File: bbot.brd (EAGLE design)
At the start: 61.5 x 53.3 mm, 27 parts

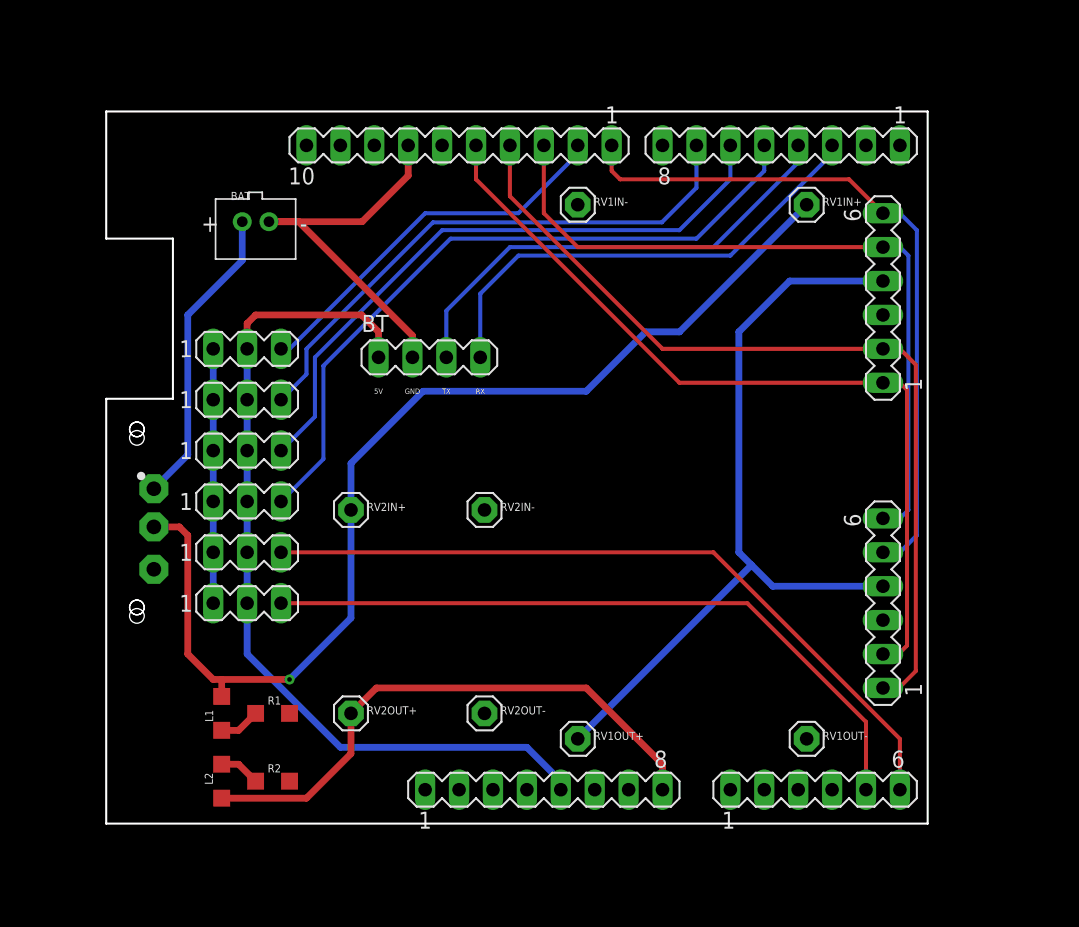
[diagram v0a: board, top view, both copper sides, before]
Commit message: added lm2596, everything is working
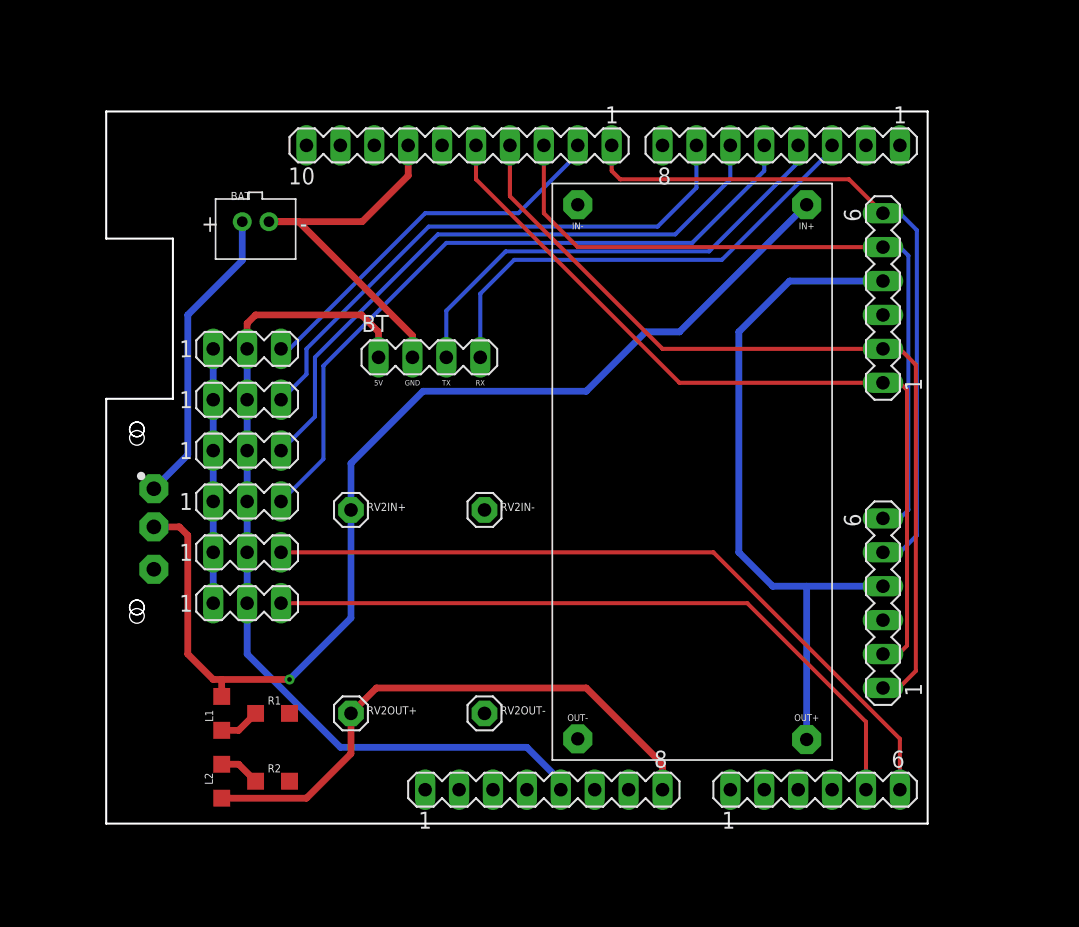
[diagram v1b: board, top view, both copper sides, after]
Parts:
- removed RV1IN+, RV1IN-, RV1OUT+, RV1OUT-: (no value), adafruit:1X01
- added U$1: BB-LM2596, my-library:BB-LM2596
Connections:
- net 5V: now also U$1.OUT+; no longer RV1OUT+.1
- net 7.4V: now also U$1.IN+; no longer RV1IN+.1
- net GND: now also U$1.IN-, U$1.OUT-; no longer RV1IN-.1, RV1OUT-.1
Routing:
- net 5V: track 59.1 -> 52.2 mm
- net N$15: track 48.5 -> 47.2 mm
- net N$16: track 53.7 -> 52.4 mm

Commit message: added some tags to brd
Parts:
- removed RV2IN+, RV2IN-, RV2OUT+, RV2OUT-: (no value), adafruit:1X01
- removed SV1, SV10, SV2, SV3, SV4, SV9: (no value), con-lstb:MA03-1
- added 4, 5, 6, 9, A0, A1: BB-PIN3, my-library:BB-PIN3
- added LM2596MINI: BB-LM2596MINI, my-library:BB-LM2596MINI
- BT: value 5V -> (none)
- renumbered U$1 to LM2596
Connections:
- net 5V-A: now also 4.2, 5.2, 6.2, 9.2, A0.2, A1.2; no longer SV1.2, SV10.2, SV2.2, SV3.2, SV4.2, SV9.2
- net 7.4V: now also LM2596MINI.IN+; no longer RV2IN+.1
- net GND: now also 4.1, 5.1, 6.1, 9.1, A0.1, A1.1, LM2596MINI.IN-, LM2596MINI.OUT-; no longer RV2IN-.1, RV2OUT-.1, SV1.1, SV10.1, SV2.1, SV3.1, SV4.1, SV9.1
- net N$14: now also 6.3; no longer SV2.3
- net N$15: now also 5.3; no longer SV3.3
- net N$16: now also 4.3; no longer SV4.3
- net N$17: now also A1.3, SV8.2; no longer SV8.6, SV9.3
- net N$18: now also A0.3, SV8.1; no longer SV10.3, SV8.5
- net N$5: now also 9.3; no longer SV1.3
- net VIN: now also LM2596MINI.OUT+; no longer RV2OUT+.1
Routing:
- net GND: track 49.1 -> 20.8 mm
- net N$17: track 56.0 -> 45.0 mm
- net N$18: track 52.6 -> 41.7 mm
- net VIN: track 42.5 -> 43.3 mm
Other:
- board text added: "ARDUINO"
- board text added: "BATERÍA"

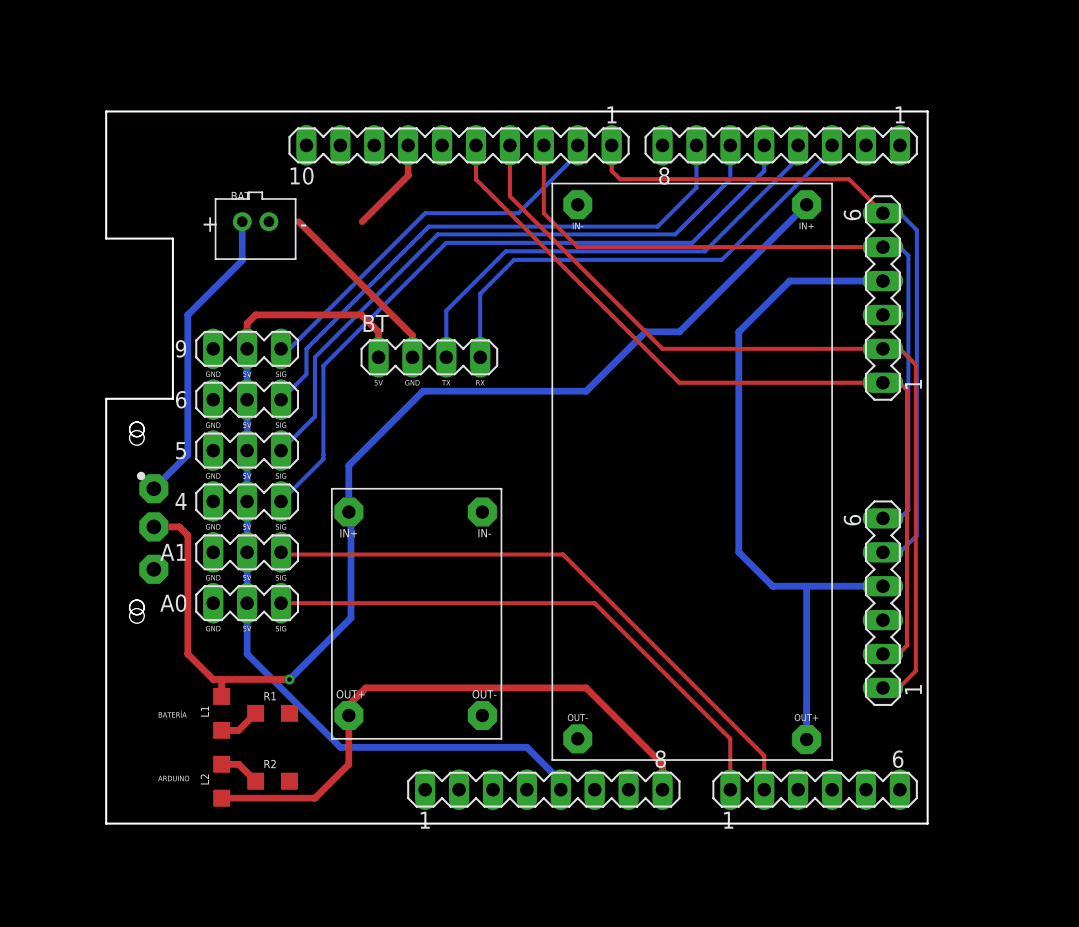
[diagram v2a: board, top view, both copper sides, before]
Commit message: changed footprint arduino and h bridge, and added more tags
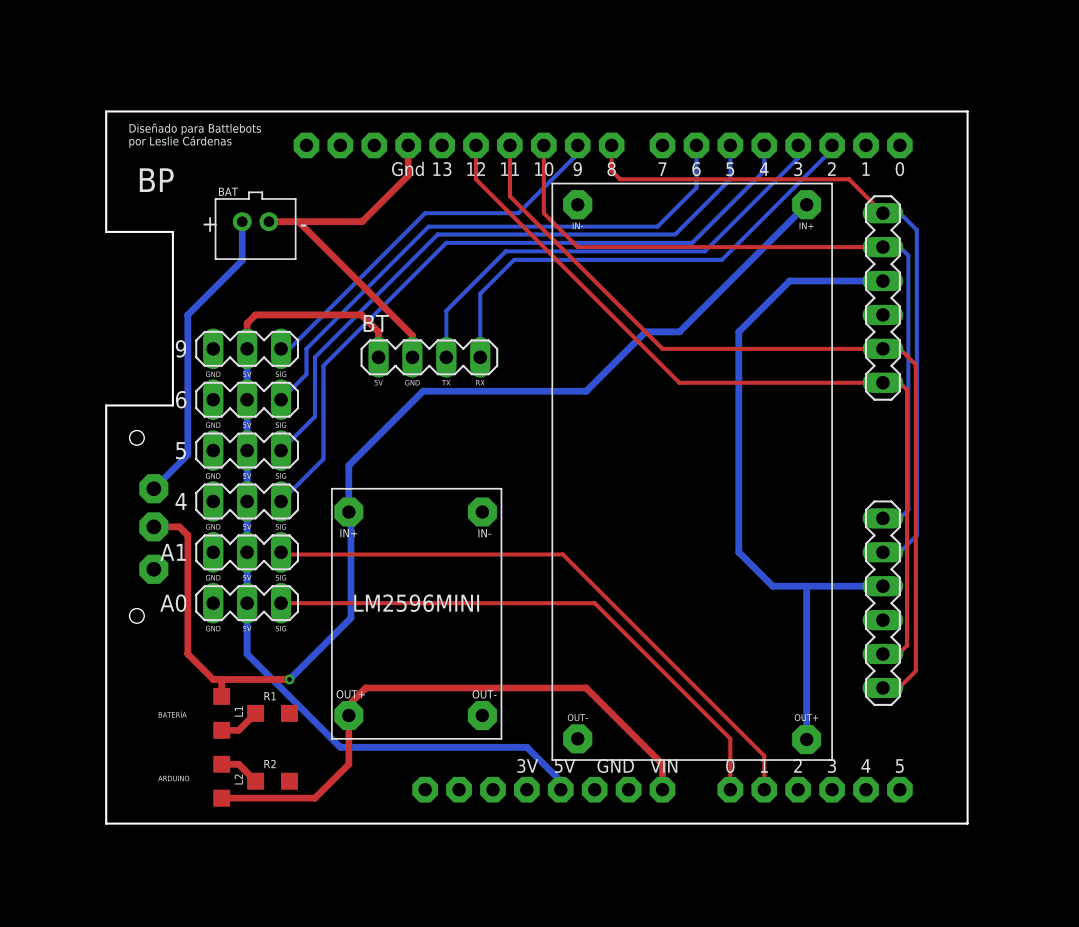
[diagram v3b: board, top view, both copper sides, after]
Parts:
- removed D1, D2, SV8: (no value), con-lstb:MA06-1
- removed SV5: (no value), con-lstb:MA10-1
- removed SV6, SV7: (no value), con-lstb:MA08-1
- added U$1: BB-ARD, my-library:BB-ARD
- added U$2, U$3: BB-PTEH, my-library:BB-PTEH
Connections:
- net 5V: now also U$2.VCC, U$3.VCC; no longer D1.4, D2.4
- net 5V-A: now also U$1.5V; no longer SV7.5
- net GND: now also U$1.GND, U$1.GND1, U$1.GND2, U$2.GND, U$3.GND; no longer D1.3, D2.3, SV5.7, SV7.6, SV7.7
- net N$1: now also U$1.D3; no longer SV6.4
- net N$11: now also U$1.D12, U$2.B1A, U$3.B1B; no longer D1.2, D2.1, SV5.5
- net N$12: now also U$1.D10, U$2.A1A, U$3.A1B; no longer D1.6, D2.5, SV5.3
- net N$13: now also U$1.D8, U$2.A1B, U$3.A1A; no longer D1.5, D2.6, SV5.1
- net N$14: now also U$1.D6; no longer SV6.7
- net N$15: now also U$1.D5; no longer SV6.6
- net N$16: now also U$1.D4; no longer SV6.5
- net N$17: now also U$1.A1; no longer SV8.2
- net N$18: now also U$1.A0; no longer SV8.1
- net N$5: now also U$1.D9; no longer SV5.2
- net N$8: now also U$1.D11, U$2.B1B, U$3.B1A; no longer D1.1, D2.2, SV5.4
- net N$9: now also U$1.D2; no longer SV6.3
- net VIN: now also U$1.VIN; no longer SV7.8
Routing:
- net GND: track 20.8 -> 27.8 mm
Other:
- board size 61.5 x 53.3 mm -> 64.5 x 53.3 mm
- board text added: "BP"
- board text added: "Diseñado para BattleBots 2022 por Leslie C."
- board text added: "Diseñado para Battlebots"
- board text added: "por Leslie Cárdenas"

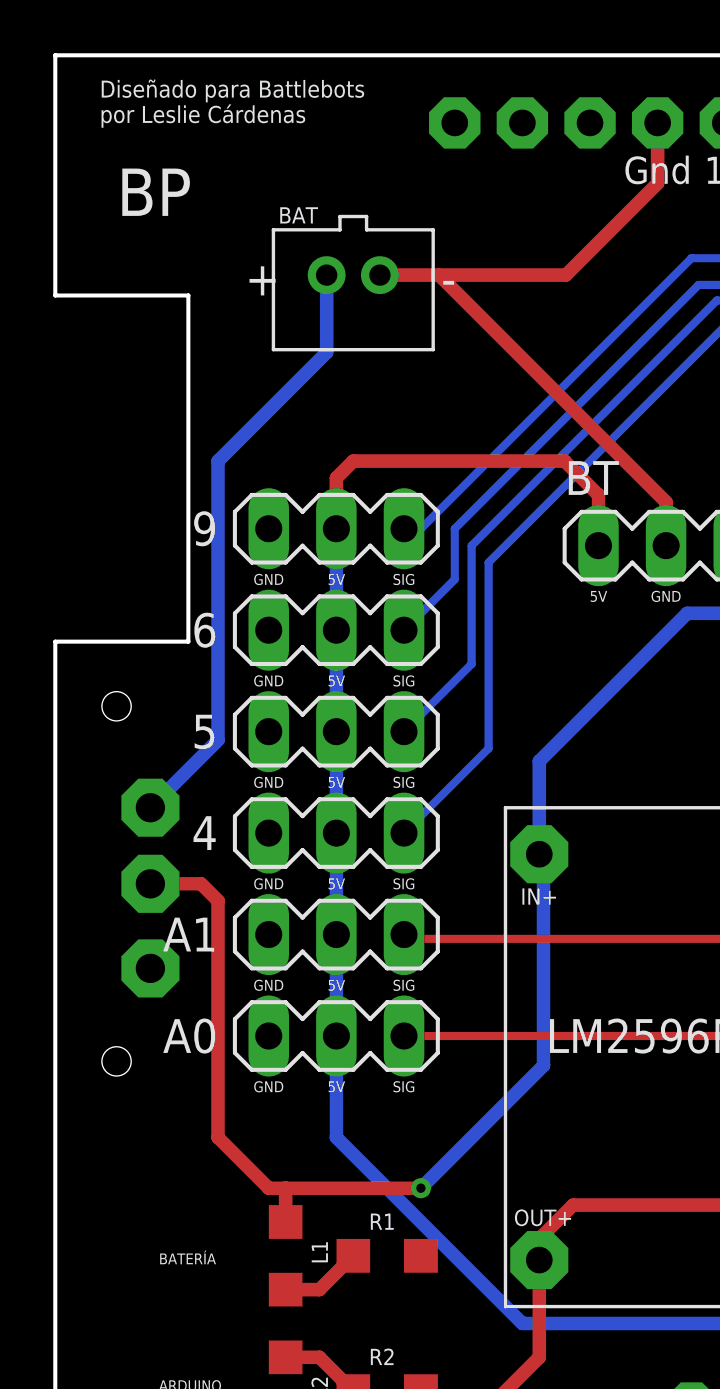
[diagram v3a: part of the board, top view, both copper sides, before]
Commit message: added bp label and diode
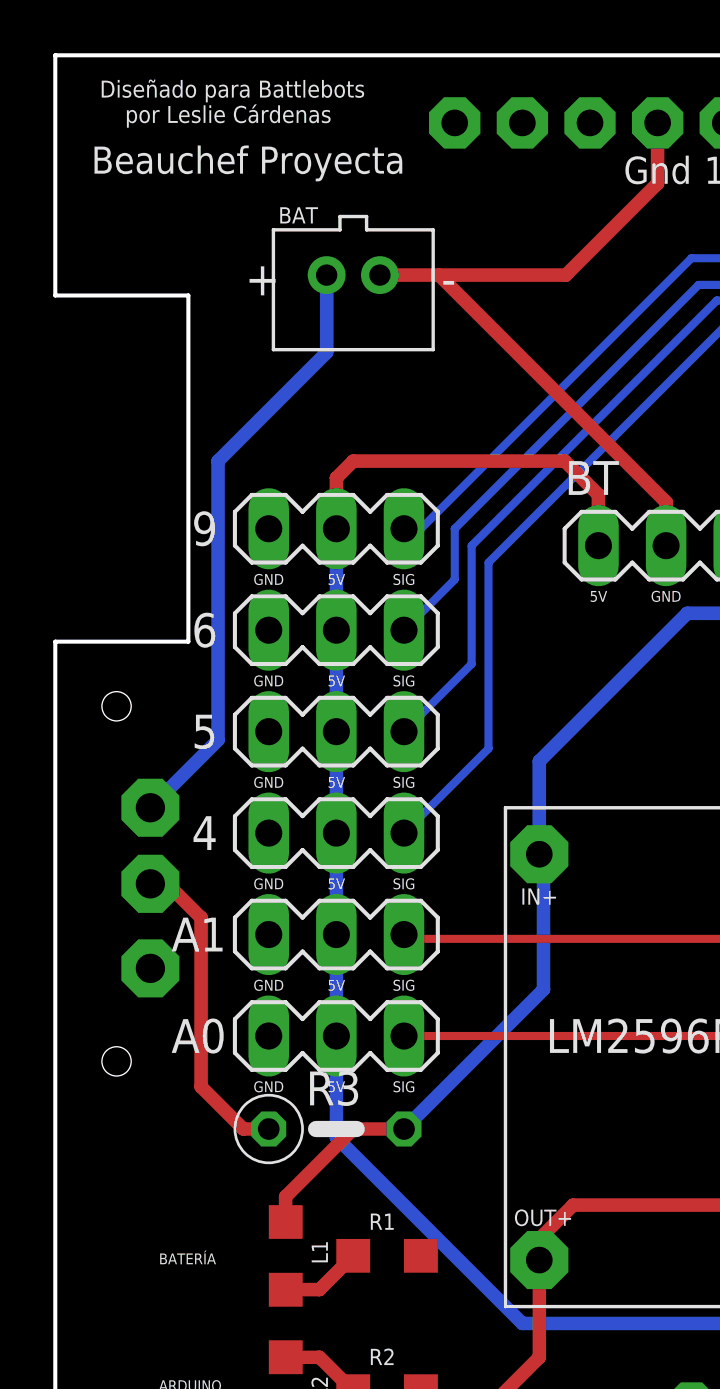
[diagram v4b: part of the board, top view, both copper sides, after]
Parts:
- added R3: (no value), rcl:0207/5V
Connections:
- new net N$2: R3.1, SW1.2
- net 7.4V: now also R3.2; no longer SW1.2
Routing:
- net 7.4V: track 81.8 -> 64.9 mm, vias 1 -> 0
- net N$2: track 0.00 -> 12.0 mm
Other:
- board text added: "Beauchef Proyecta"
- board text removed: "BP"
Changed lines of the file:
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@@
 <wire x1="-30.2412" y1="4.65" x2="-25.243" y2="4.65" width="0.1524" layer="20" locked="yes"/>
 <text x="-28.575" y="25.0825" size="0.635" layer="21">Diseñado para Battlebots</text>
-<text x="-28.575" y="24.13" size="0.635" layer="21">por Leslie Cárdenas</text>
-<text x="-27.94" y="20.6375" size="1.778" layer="21">BP</text>
+<text x="-27.6225" y="24.13" size="0.635" layer="21">por Leslie Cárdenas</text>
+<text x="-28.8925" y="22.225" size="1.016" layer="21">Beauchef Proyecta</text>
 </plain>
 <attributes>
@@
 <element name="A1" library="my-library" library_urn="urn:adsk.eagle:library:37248401" package="BB-PIN3" value="BB-PIN3" x="-19.685" y="-6.35" smashed="yes">
 <attribute name="NAME" x="-15.5575" y="-6.35" size="1.27" layer="25" ratio="10" align="center-left"/>
-<attribute name="NAME" x="-24.13" y="-6.35" size="1.27" layer="25" ratio="10" align="center-right"/>
+<attribute name="NAME" x="-23.8125" y="-6.35" size="1.27" layer="25" ratio="10" align="center-right"/>
 </element>
 <element name="A0" library="my-library" library_urn="urn:adsk.eagle:library:37248401" package="BB-PIN3" value="BB-PIN3" x="-19.685" y="-10.16" smashed="yes">
 <attribute name="NAME" x="-15.24" y="-10.16" size="1.27" layer="25" ratio="10" align="center-left"/>
-<attribute name="NAME" x="-24.13" y="-10.16" size="1.27" layer="25" ratio="10" align="center-right"/>
+<attribute name="NAME" x="-23.8125" y="-10.16" size="1.27" layer="25" ratio="10" align="center-right"/>
 </element>
 <element name="4" library="my-library" library_urn="urn:adsk.eagle:library:37248401" package="BB-PIN3" value="BB-PIN3" x="-19.685" y="-2.54" smashed="yes">
@@
 <element name="U$2" library="my-library" library_urn="urn:adsk.eagle:library:37248401" package="BB-PTEH" value="BB-PTEH" x="27.94" y="12.7" smashed="yes" rot="R90"/>
 <element name="U$3" library="my-library" library_urn="urn:adsk.eagle:library:37248401" package="BB-PTEH" value="BB-PTEH" x="27.94" y="-10.16" smashed="yes" rot="R90"/>
+<element name="R3" library="rcl" library_urn="urn:adsk.eagle:library:334" package="0207/5V" package3d_urn="urn:adsk.eagle:package:23502/1" value="" x="-19.685" y="-13.6525" smashed="yes">
+<attribute name="NAME" x="-20.828" y="-12.7635" size="1.27" layer="25" ratio="10"/>
+<attribute name="POPULARITY" value="4" x="-19.685" y="-13.6525" size="1.778" layer="27" display="off"/>
+<attribute name="SPICEPREFIX" value="R" x="-19.685" y="-13.6525" size="1.778" layer="27" display="off"/>
+<attribute name="VALUE" x="-20.828" y="-15.8115" size="1.27" layer="27" ratio="10"/>
+</element>
 </elements>
 <signals>
@@
 </signal>
 <signal name="7.4V">
-<contactref element="SW1" pad="2"/>
-<wire x1="-22.225" y1="-15.875" x2="-21.59" y2="-15.875" width="0.508" layer="1"/>
-<wire x1="-21.59" y1="-15.875" x2="-16.51" y2="-15.875" width="0.508" layer="1"/>
-<wire x1="-26.67" y1="-4.445" x2="-24.765" y2="-4.445" width="0.508" layer="1"/>
-<wire x1="-24.765" y1="-4.445" x2="-24.13" y2="-5.08" width="0.508" layer="1"/>
-<wire x1="-24.13" y1="-5.08" x2="-24.13" y2="-13.97" width="0.508" layer="1"/>
-<wire x1="-24.13" y1="-13.97" x2="-22.225" y2="-15.875" width="0.508" layer="1"/>
-<via x="-16.51" y="-15.875" extent="1-16" drill="0.35"/>
-<wire x1="-16.51" y1="-15.875" x2="-11.90625" y2="-11.27125" width="0.508" layer="16"/>
+<wire x1="-17.145" y1="-13.6525" x2="-11.90625" y2="-8.41375" width="0.508" layer="16"/>
 <contactref element="LM2596" pad="IN+"/>
 <contactref element="L1" pad="2"/>
@@
 <wire x1="12.7" y1="10.16" x2="22.225" y2="19.685" width="0.508" layer="16"/>
 <contactref element="LM2596MINI" pad="IN+"/>
-<wire x1="-11.90625" y1="-11.27125" x2="-11.90625" y2="-3.4925" width="0.508" layer="16"/>
+<wire x1="-11.90625" y1="-8.41375" x2="-11.90625" y2="-3.4925" width="0.508" layer="16"/>
 <wire x1="-11.90625" y1="-3.4925" x2="-12.065" y2="-3.33375" width="0.508" layer="16"/>
 <wire x1="-12.065" y1="-3.33375" x2="-12.065" y2="0.15875" width="0.508" layer="16"/>
 <wire x1="-12.065" y1="0.15875" x2="-6.50875" y2="5.715" width="0.508" layer="16"/>
-<wire x1="-21.59" y1="-17.145" x2="-21.59" y2="-15.875" width="0.508" layer="1"/>
+<wire x1="-21.59" y1="-17.145" x2="-21.59" y2="-16.1925" width="0.508" layer="1"/>
+<contactref element="R3" pad="2"/>
+<wire x1="-21.59" y1="-16.1925" x2="-19.05" y2="-13.6525" width="0.508" layer="1"/>
+<wire x1="-19.05" y1="-13.6525" x2="-17.145" y2="-13.6525" width="0.508" layer="1"/>
 </signal>
 <signal name="N$9">
@@
 <wire x1="21.59" y1="24.13" x2="21.59" y2="23.1775" width="0.3048" layer="16"/>
 </signal>
+<signal name="N$2">
+<contactref element="SW1" pad="2"/>
+<contactref element="R3" pad="1"/>
+<wire x1="-26.67" y1="-4.445" x2="-26.035" y2="-4.445" width="0.508" layer="1"/>
+<wire x1="-26.035" y1="-4.445" x2="-24.765" y2="-5.715" width="0.508" layer="1"/>
+<wire x1="-24.765" y1="-5.715" x2="-24.765" y2="-12.065" width="0.508" layer="1"/>
+<wire x1="-24.765" y1="-12.065" x2="-23.1775" y2="-13.6525" width="0.508" layer="1"/>
+<wire x1="-23.1775" y1="-13.6525" x2="-22.225" y2="-13.6525" width="0.508" layer="1"/>
+</signal>
 </signals>
